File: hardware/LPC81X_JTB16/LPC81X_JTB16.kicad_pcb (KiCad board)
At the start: 2 copper layers, 2 parts

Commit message: WIP schematic definition and raw component placement
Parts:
- added J1: Conn_01x08, SquantorConnectors:Header-0254-1X08-H010, F.Cu at (147.3, 80.0)
- added J2: Conn_01x08, SquantorConnectors:Header-0254-1X08-H010, F.Cu at (154.9, 80.0)
- added U1: LPC812M101JTB16, Package_SON:NXP_XSON-16, F.Cu at (151.1, 80.0)
- N1: value 20200610 -> 20200720

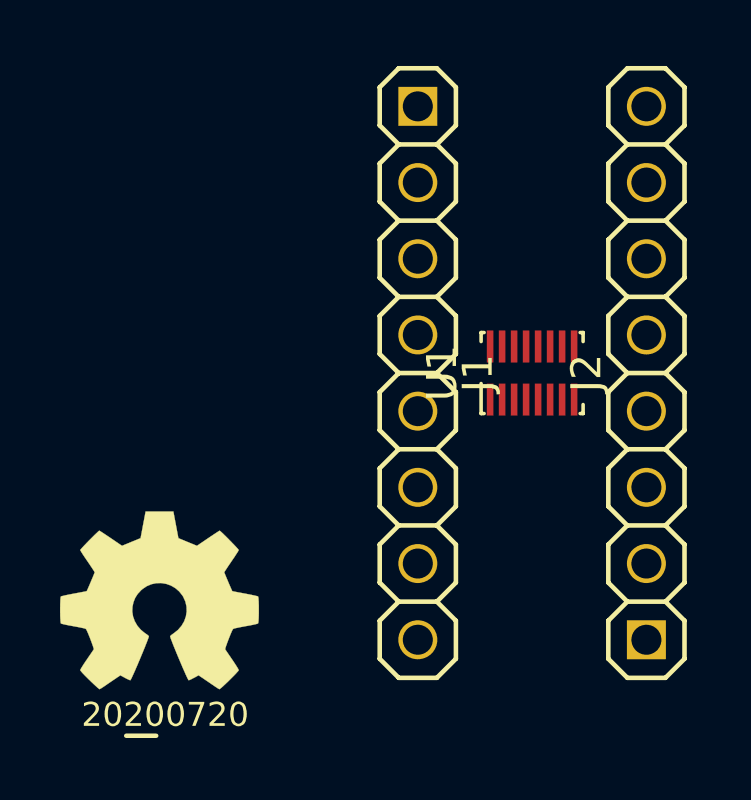
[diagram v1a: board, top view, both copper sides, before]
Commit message: further schematic definition and component placement
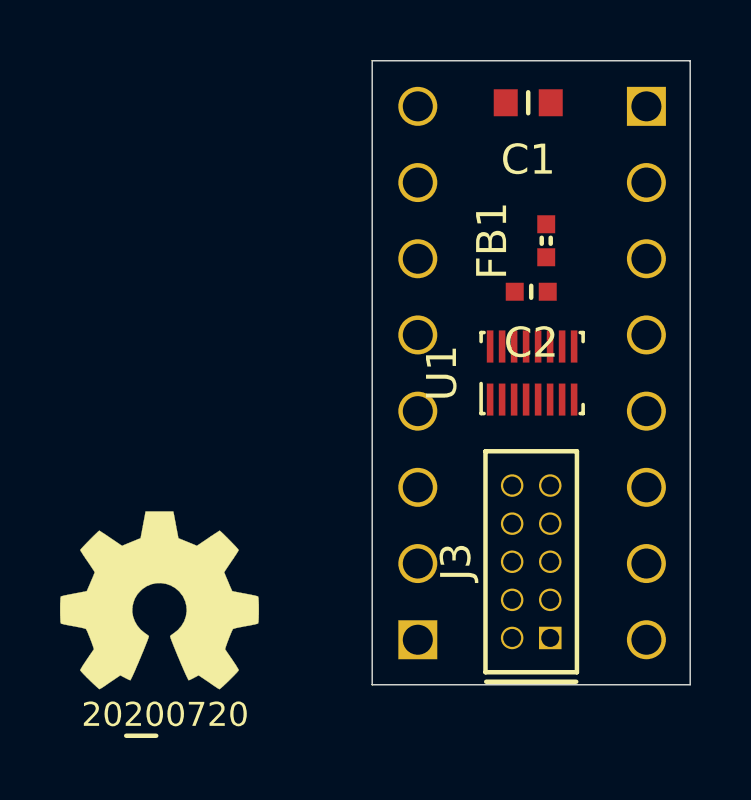
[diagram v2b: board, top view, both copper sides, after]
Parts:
- added C1: 10u, SquantorRcl:C_0603, F.Cu at (151.0, 71.0)
- added C2: 1u, SquantorRcl:C_0402, F.Cu at (151.1, 77.3)
- added FB1: 600, SquantorRcl:L_0402, F.Cu at (151.6, 75.6)
- added J3: JTAG_2X05_IN, SquantorConnectors:Header-0127-2X05-H006, F.Cu at (151.1, 86.3)
- J1, J2: moved to B.Cu
- turned J1 to 90 degrees
- turned J2 to 270 degrees
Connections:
- net Net-(U1-Pad10) renamed /PIO0_9
- net Net-(U1-Pad11) renamed /PIO0_8
- net Net-(U1-Pad14) renamed /PIO0_7
- net Net-(U1-Pad15) renamed /PIO0_6
- net Net-(U1-Pad16) renamed /PIO0_0
- net Net-(U1-Pad9) renamed /PIO0_1
- J1 pad 1: Net-(J1-Pad1) -> /PIO0_4
- J1 pad 2: Net-(J1-Pad2) -> /PIO0_5
- J1 pad 3: Net-(J1-Pad3) -> /PIO0_12
- J1 pad 4: Net-(J1-Pad4) -> /PIO0_13
- J2 pad 5: Net-(J2-Pad5) -> /PIO0_10
- J2 pad 6: Net-(J2-Pad6) -> /PIO0_11
- J2 pad 7: Net-(J2-Pad7) -> /PIO0_2
- J2 pad 8: Net-(J2-Pad8) -> /PIO0_3
- U1 pad 1: Net-(U1-Pad1) -> /PIO0_13
- U1 pad 13: Net-(U1-Pad13) -> /VSS
- U1 pad 2: Net-(U1-Pad2) -> /PIO0_12
- U1 pad 3: Net-(U1-Pad3) -> /PIO0_5
- U1 pad 4: Net-(U1-Pad4) -> /PIO0_4
- U1 pad 5: Net-(U1-Pad5) -> /PIO0_3
- U1 pad 6: Net-(U1-Pad6) -> /PIO0_2
- U1 pad 7: Net-(U1-Pad7) -> /PIO0_11
- U1 pad 8: Net-(U1-Pad8) -> /PIO0_10
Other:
- board outline added: 10.6 x 20.8 mm
